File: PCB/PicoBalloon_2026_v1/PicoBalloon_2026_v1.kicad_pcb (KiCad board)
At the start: 2 copper layers, 20 x 30 mm, 51 parts, among them J1 Conn_01x07_Pin, J10 Conn_01x02_Pin, J11 Conn_01x01_Pin, J12 Conn_01x01_Pin, J2 Conn_01x04_Pin, J3 Conn_01x01_Pin, J4 Conn_01x02_Pin, J5 Conn_01x02_Pin, J6 Conn_01x02_Pin, J7 Conn_01x02_Pin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

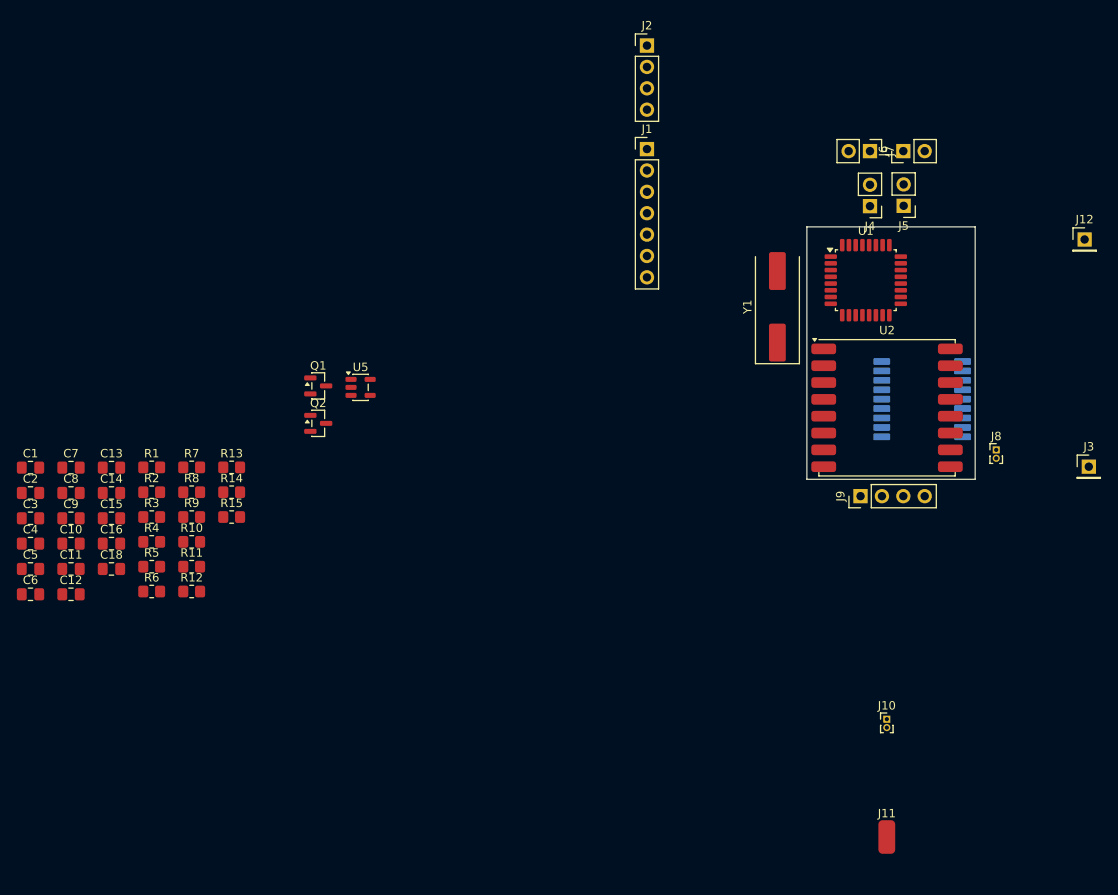
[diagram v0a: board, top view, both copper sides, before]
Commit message: [PCB] PCB finished! (I hope). Not so critical signals removed. Voltage regulator removed because it is not needed.
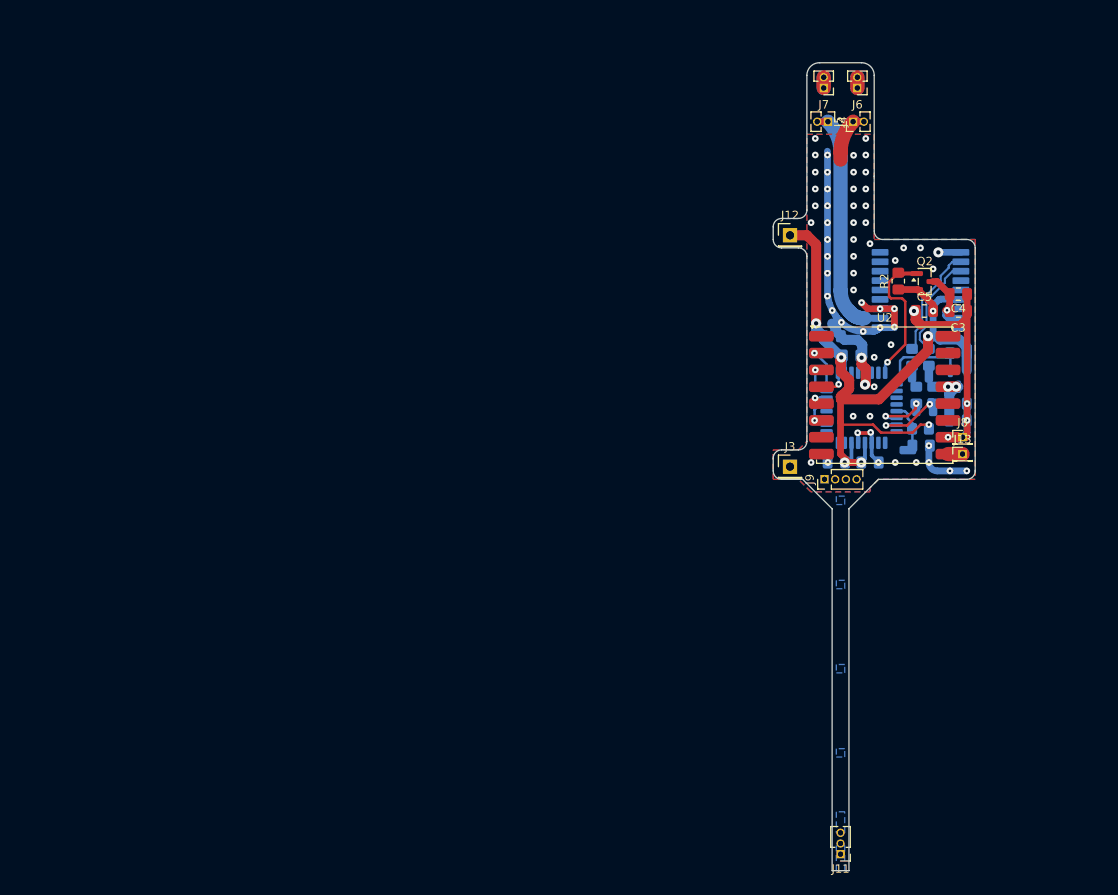
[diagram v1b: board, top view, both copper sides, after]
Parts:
- removed C10, C7: 2u2, Capacitor_SMD:C_0805_2012Metric_Pad1.18x1.45mm_HandSolder
- removed C11, C12: 22p, Capacitor_SMD:C_0805_2012Metric_Pad1.18x1.45mm_HandSolder
- removed C6, C9: 100n, Capacitor_SMD:C_0805_2012Metric_Pad1.18x1.45mm_HandSolder
- removed C8: 470pF, Capacitor_SMD:C_0805_2012Metric_Pad1.18x1.45mm_HandSolder
- removed J10: Conn_01x02_Pin, Connector_PinHeader_1.00mm:PinHeader_1x02_P1.00mm_Vertical
- removed J2: Conn_01x04_Pin, Connector_PinHeader_2.54mm:PinHeader_1x04_P2.54mm_Vertical
- removed R11: 10k, Resistor_SMD:R_0805_2012Metric_Pad1.20x1.40mm_HandSolder
- removed R12, R13, R14, R15, R4, R5: *np, Resistor_SMD:R_0805_2012Metric_Pad1.20x1.40mm_HandSolder
- removed R3: 0R0, Resistor_SMD:R_0805_2012Metric_Pad1.20x1.40mm_HandSolder
- removed U5: TS5205CX525, Package_TO_SOT_SMD:SOT-23-5
- removed Y1: 8MHz, Crystal:Crystal_SMD_HC49-SD
- added J13: Conn_01x01_Pin, Connector_PinHeader_1.27mm:PinHeader_1x01_P1.27mm_Vertical, F.Cu at (150.0, 99.5)
- added J14: Conn_01x01_Pin, Connector_Wire:SolderWirePad_1x01_SMD_1x2mm, B.Cu at (143.5, 99.0)
- added J15: Conn_01x01_Pin, Connector_Wire:SolderWirePad_1x01_SMD_1x2mm, B.Cu at (146.5, 94.0)
- added J16: Conn_01x01_Pin, Connector_Wire:SolderWirePad_1x01_SMD_1x2mm, B.Cu at (144.0, 90.0)
- added J17: Conn_01x01_Pin, Connector_Wire:SolderWirePad_1x01_SMD_1x2mm, B.Cu at (146.0, 90.0)
- C1, C13, C14, C15, C16, C18, C2, Q1, R1, R6, R7, R8, R9, U1: moved to B.Cu
- J1: value Conn_01x07_Pin -> Conn_01x01_Pin; footprint Connector_PinHeader_2.54mm:PinHeader_1x07_P2.54mm_Vertical -> Connector_Wire:SolderWirePad_1x01_SMD_1x2mm; moved to B.Cu
- J11: value Conn_01x01_Pin -> Conn_01x03_Pin; footprint Connector_Wire:SolderWirePad_1x01_SMD_2x4mm -> Connector_PinHeader_1.27mm:PinHeader_1x03_P1.27mm_Vertical
- J4, J5, J6, J7: footprint Connector_PinHeader_2.54mm:PinHeader_1x02_P2.54mm_Vertical -> Connector_PinHeader_1.27mm:PinHeader_1x02_P1.27mm_Vertical
- J8: value Conn_01x02_Pin -> Conn_01x01_Pin; footprint Connector_PinHeader_1.00mm:PinHeader_1x02_P1.00mm_Vertical -> Connector_PinHeader_1.27mm:PinHeader_1x01_P1.27mm_Vertical
- J9: footprint Connector_PinHeader_2.54mm:PinHeader_1x04_P2.54mm_Vertical -> Connector_PinHeader_1.27mm:PinHeader_1x04_P1.27mm_Vertical
- R10: value *np -> 10k; moved to B.Cu
- moved C4 114.2 mm to (149.5, 80.5), turned to 180 degrees
- moved C3 113.0 mm to (149.5, 82.5), turned to 180 degrees
- moved C2 110.5 mm to (149.5, 95.5), turned to 180 degrees
- moved C5 110.5 mm to (145.5, 82.5)
- moved C1 110.5 mm to (149.5, 93.5), turned to 180 degrees
- moved C18 97.3 mm to (145.1, 98.5), turned to 180 degrees
- moved R1 96.8 mm to (149.5, 87.5), turned to 180 degrees
- moved R6 93.4 mm to (145.0, 96.5)
- moved R2 92.2 mm to (142.4, 79.0), turned to 90 degrees
- moved R10 90.3 mm to (146.0, 88.0), turned to 90 degrees
- moved C14 90.2 mm to (139.0, 100.5), turned to 180 degrees
- moved C15 90.0 mm to (136.8, 87.8), turned to 180 degrees
- moved R9 89.3 mm to (146.5, 92.5), turned to 90 degrees
- moved C16 89.1 mm to (134.5, 85.5), turned to 180 degrees
- moved R8 87.1 mm to (144.0, 88.0), turned to 90 degrees
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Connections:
- net Net-(Q1-D) renamed /LORA_VCC
- net Net-(Q2-D) renamed /GPS_VCC
- J1 pad 1: GND -> /MCU_RX
- J11 pad 1: Net-(J10-Pin_2) -> Net-(J11-Pin_1)
- U1 pad 1: Net-(U1-PD3) -> unconnected-(U1-PD3-Pad1)
- U1 pad 12: /PWR1_ENn -> unconnected-(U1-PB0-Pad12)
- U1 pad 19: /ADC_IN_2V5 -> unconnected-(U1-ADC6-Pad19)
- U1 pad 2: Net-(U1-PD4) -> unconnected-(U1-PD4-Pad2)
- U1 pad 20: /ADC_REF -> unconnected-(U1-AREF-Pad20)
- U1 pad 23: Net-(J2-Pin_4) -> unconnected-(U1-PC0-Pad23)
- U1 pad 24: Net-(J2-Pin_3) -> /PWR2_ENn
- U1 pad 25: Net-(J2-Pin_2) -> /PWR1_ENn
- U1 pad 26: Net-(J2-Pin_1) -> unconnected-(U1-PC3-Pad26)
- U1 pad 32: Net-(U1-PD2) -> unconnected-(U1-PD2-Pad32)
- U1 pad 7: Net-(U1-XTAL1/PB6) -> unconnected-(U1-XTAL1/PB6-Pad7)
- U1 pad 8: Net-(U1-XTAL2/PB7) -> unconnected-(U1-XTAL2/PB7-Pad8)
- U1 pad 9: /PWR2_ENn -> unconnected-(U1-PD5-Pad9)
- U2 pad 6: Net-(U2-RESET) -> /LORA_RESETn
- U3 pad 13: Net-(U3-IO8) -> unconnected-(U3-IO8-Pad13)
- U3 pad 4: Net-(U3-PPS) -> unconnected-(U3-PPS-Pad4)
- U3 pad 5: Net-(U3-N/F) -> unconnected-(U3-N/F-Pad5)
- U3 pad 9: Net-(U3-RST) -> unconnected-(U3-RST-Pad9)
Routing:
- net GND: track 0.00 -> 109.7 mm, vias 0 -> 66
- net VBAT: track 0.00 -> 90.8 mm, vias 0 -> 7
- net /GPS_ANT: track 0.00 -> 29.6 mm
- net /PWR2_ENn: track 0.00 -> 17.1 mm, vias 0 -> 1
- net /GPS_TX: track 0.00 -> 14.4 mm
- net /GPS_RX: track 0.00 -> 12.7 mm
- net /PWR1_ENn: track 0.00 -> 11.4 mm
- net /MCU_TX: track 0.00 -> 8.04 mm, vias 0 -> 2
- net /GPS_VCC: track 0.00 -> 7.44 mm, vias 0 -> 1
- net /LORA_VCC: track 0.00 -> 6.52 mm, vias 0 -> 2
- net /MCU_RX: track 0.00 -> 5.93 mm, vias 0 -> 2
- net /SPI_MISO: track 0.00 -> 5.18 mm, vias 0 -> 1
- net /MCU_RSTn: track 0.00 -> 4.93 mm
- net /SPI_SCK: track 0.00 -> 3.58 mm, vias 0 -> 1
- net /SPI_MOSI: track 0.00 -> 3.51 mm, vias 0 -> 1
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- added copper zone on B.Cu, net (none)
- added copper zone on B.Cu, net GND
- added copper zone on F.Cu, net GND
- added copper zone on B.Cu, net Net-(J11-Pin_1)
- added copper zone on B.Cu, net unconnected-(J11-Pin_3-Pad3)
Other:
- board size 20 x 30 mm -> 24 x 96 mm
